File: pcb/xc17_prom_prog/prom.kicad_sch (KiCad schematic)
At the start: 28 parts, among them U14 SN74LVC8T245, U15 SN74LVC8T245, U16 SN74LVC8T245, U17 XC17xxx

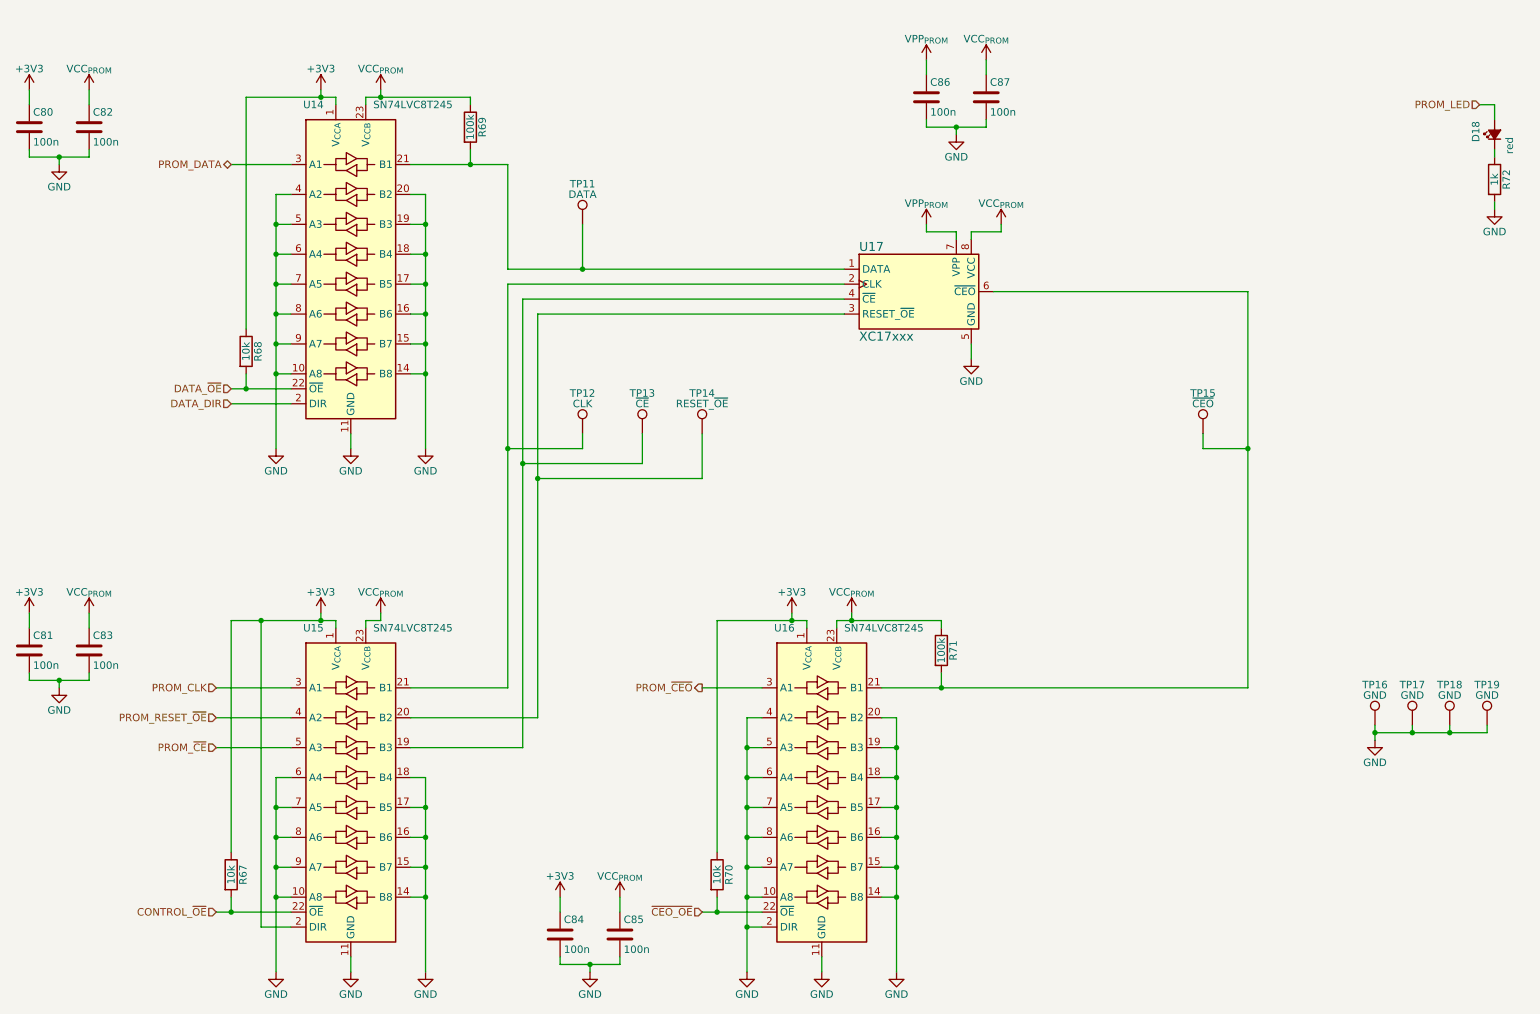
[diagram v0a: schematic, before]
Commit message: Fix MOSFETs
 * Block MOSFET body diodes by placing two MOSFETs in anti series.
 * Connect PROM LED to pin header.
 * Add transistors to actively pull PROM VCC and VPP low.
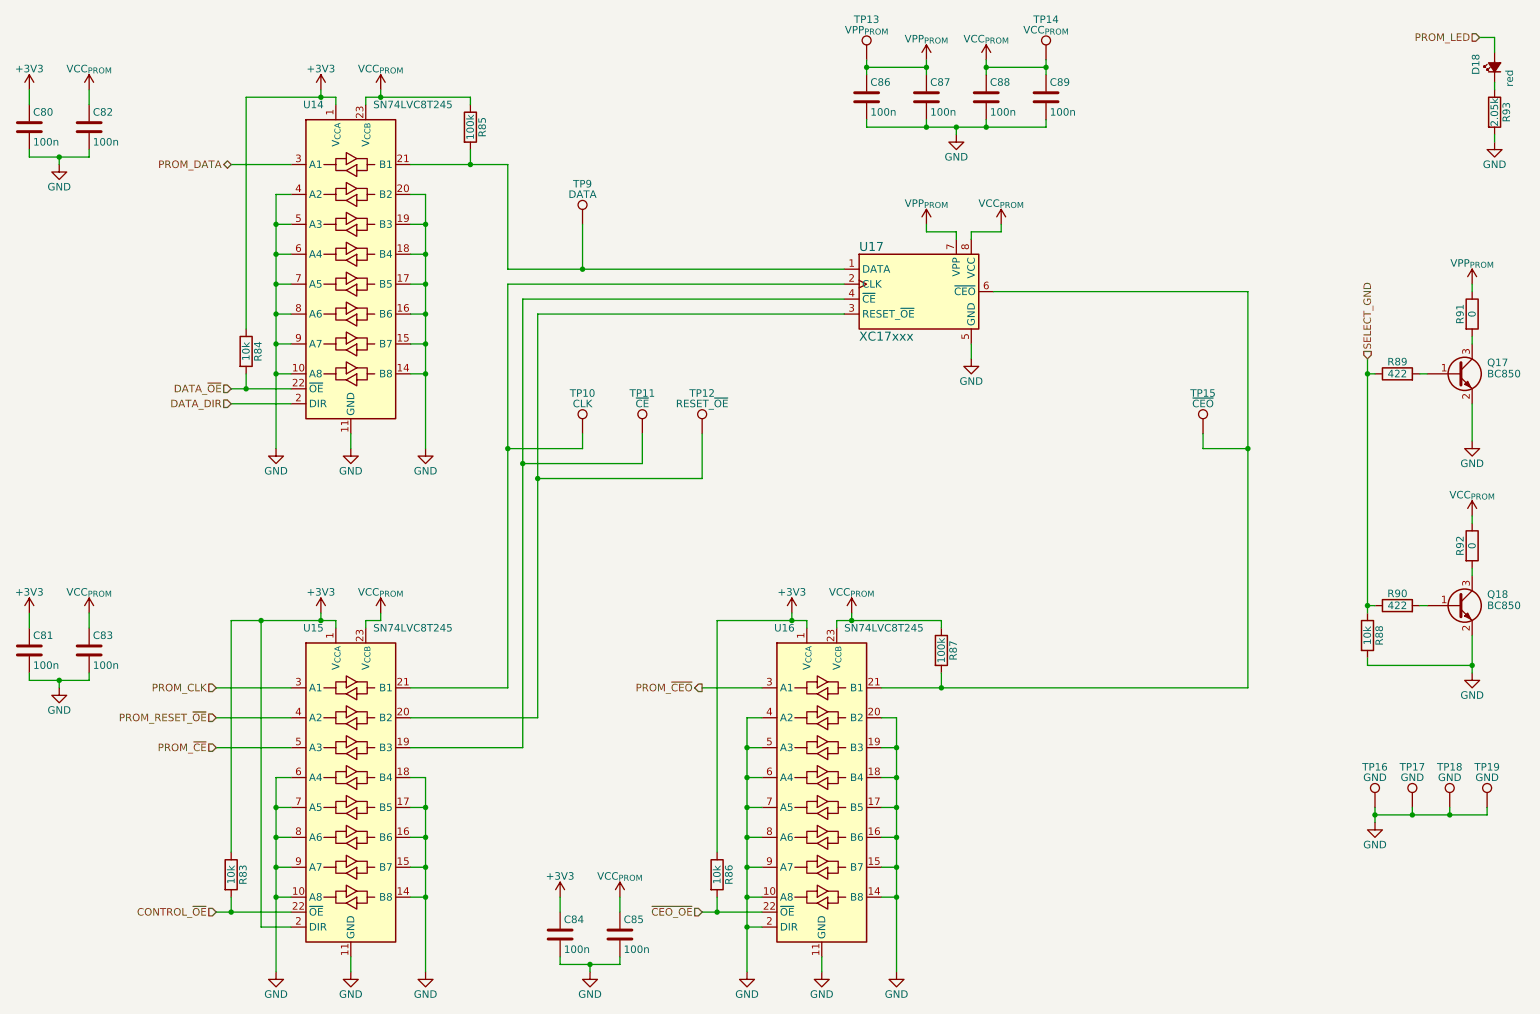
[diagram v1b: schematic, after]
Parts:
- added C86, C89: 100n, Capacitor_SMD:C_0603_1608Metric, symbol Device:C
- added Q17, Q18: BC850, Package_TO_SOT_SMD:SOT-23, symbol Transistor_BJT:BC850
- added R88: 10k, Resistor_SMD:R_0603_1608Metric, symbol Device:R
- added R89, R90: 422, Resistor_SMD:R_0603_1608Metric, symbol Device:R
- added R91, R92: 0, Resistor_SMD:R_0603_1608Metric, symbol Device:R
- added TP13: VPP_{PROM}, TestPoint:TestPoint_Keystone_5010-5014_Multipurpose, symbol Connector:TestPoint
- added TP14: VCC_{PROM}, TestPoint:TestPoint_Keystone_5010-5014_Multipurpose, symbol Connector:TestPoint
- R93: renamed from R72; value 1k -> 2.05k
- renumbered C86 to C87, C87 to C88, R67 to R83, R68 to R84, R69 to R85, R70 to R86, R71 to R87, TP12 to TP10, TP13 to TP11, TP14 to TP12, TP11 to TP9
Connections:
- net GND: now also C86.2, C89.2, Q17.2 (E), Q18.2 (E), R88.2
- net VCC_{PROM}: now also C89.1, R92.1, TP14.1
- net VPP_{PROM}: now also C86.1, R91.1, TP13.1
- new net: Q18.1 (B), R90.2
- new net: Q18.3 (C), R92.2
- new net: Q17.1 (B), R89.2
- new net: Q17.3 (C), R91.2
- new net SELECT_GND: R88.1, R89.1, R90.1
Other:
- moved on the sheet: D18, R93, TP16, TP17, TP18, TP19

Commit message: Implement more precise voltage controls
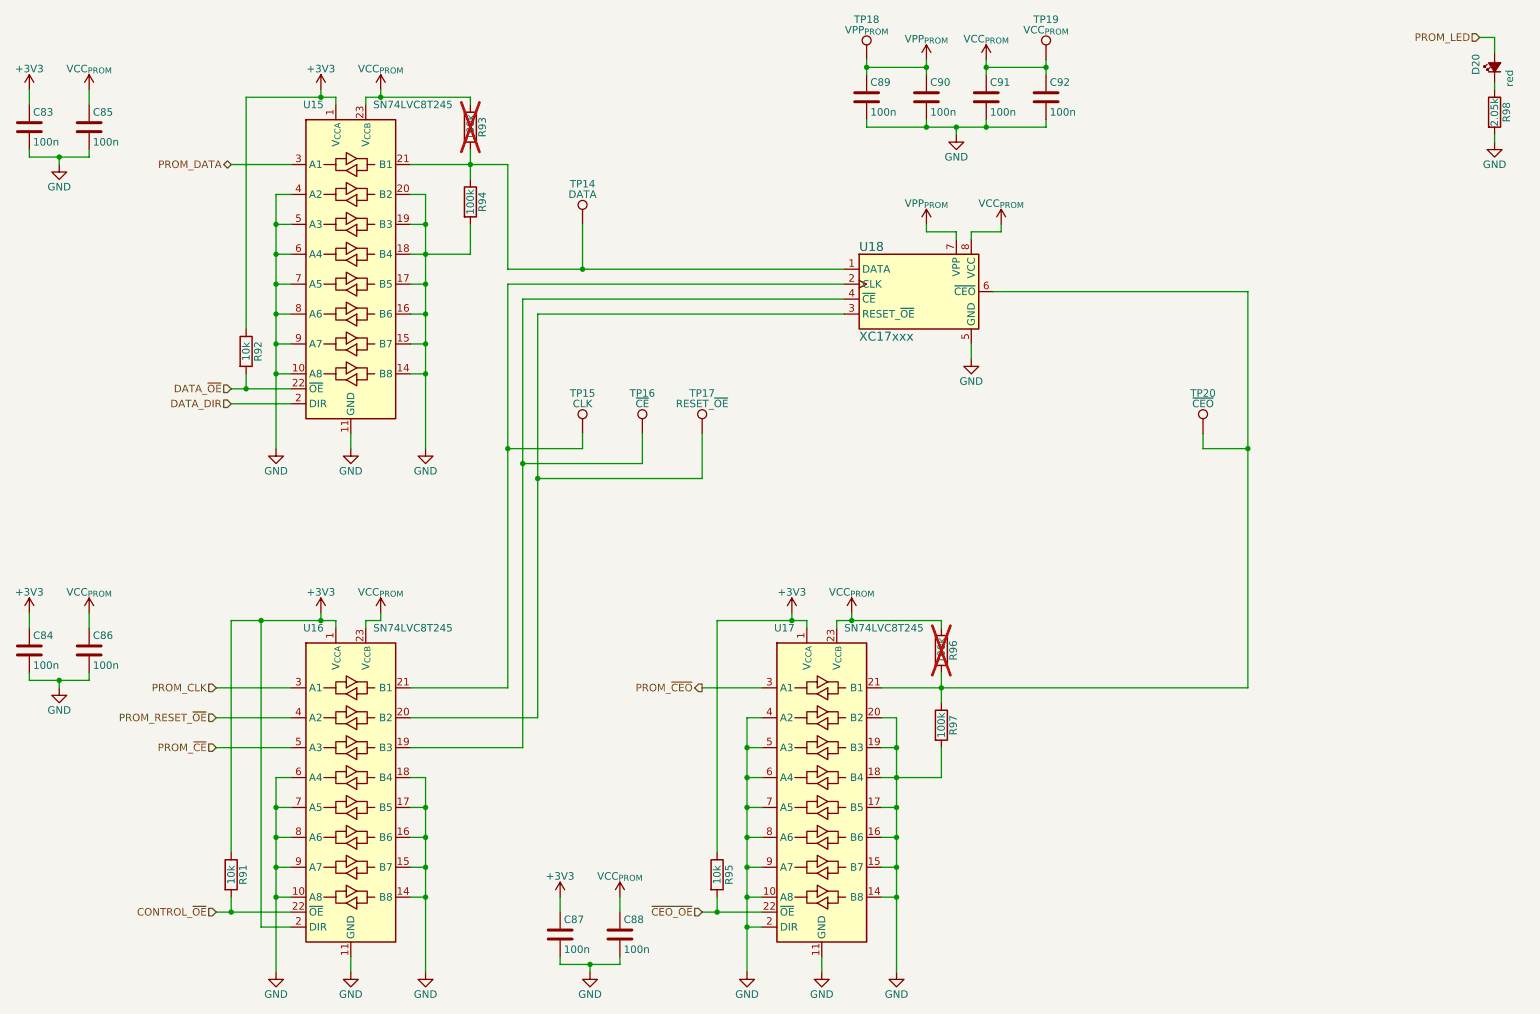
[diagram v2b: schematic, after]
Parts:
- removed Q17, Q18: BC850, Package_TO_SOT_SMD:SOT-23, symbol Transistor_BJT:BC850
- removed R88: 10k, Resistor_SMD:R_0603_1608Metric, symbol Device:R
- removed R89, R90: 422, Resistor_SMD:R_0603_1608Metric, symbol Device:R
- removed R91, R92: 0, Resistor_SMD:R_0603_1608Metric, symbol Device:R
- removed TP16, TP17, TP18, TP19: GND, TestPoint:TestPoint_Keystone_5010-5014_Multipurpose, symbol Connector:TestPoint
- added R94, R97: 100k, Resistor_SMD:R_0603_1608Metric, symbol Device:R
- R93: renamed from R85; now not fitted; now left out of the parts list
- R96: renamed from R87; now not fitted; now left out of the parts list
- renumbered C80 to C83, C81 to C84, C82 to C85, C83 to C86, C84 to C87, C85 to C88, C86 to C89, C87 to C90, C88 to C91, C89 to C92, D18 to D20, R83 to R91, R84 to R92, R86 to R95, R93 to R98, TP9 to TP14, TP10 to TP15, TP11 to TP16, TP12 to TP17, TP13 to TP18, TP14 to TP19, TP15 to TP20, U14 to U15, U15 to U16, U16 to U17, U17 to U18
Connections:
- net GND: now also R94.2, R97.2
- net at R93.2, TP14.1, U15.21 (B1)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: now also R94.1
- net at R96.2, TP20.1, U17.21 (B1)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: now also R97.1

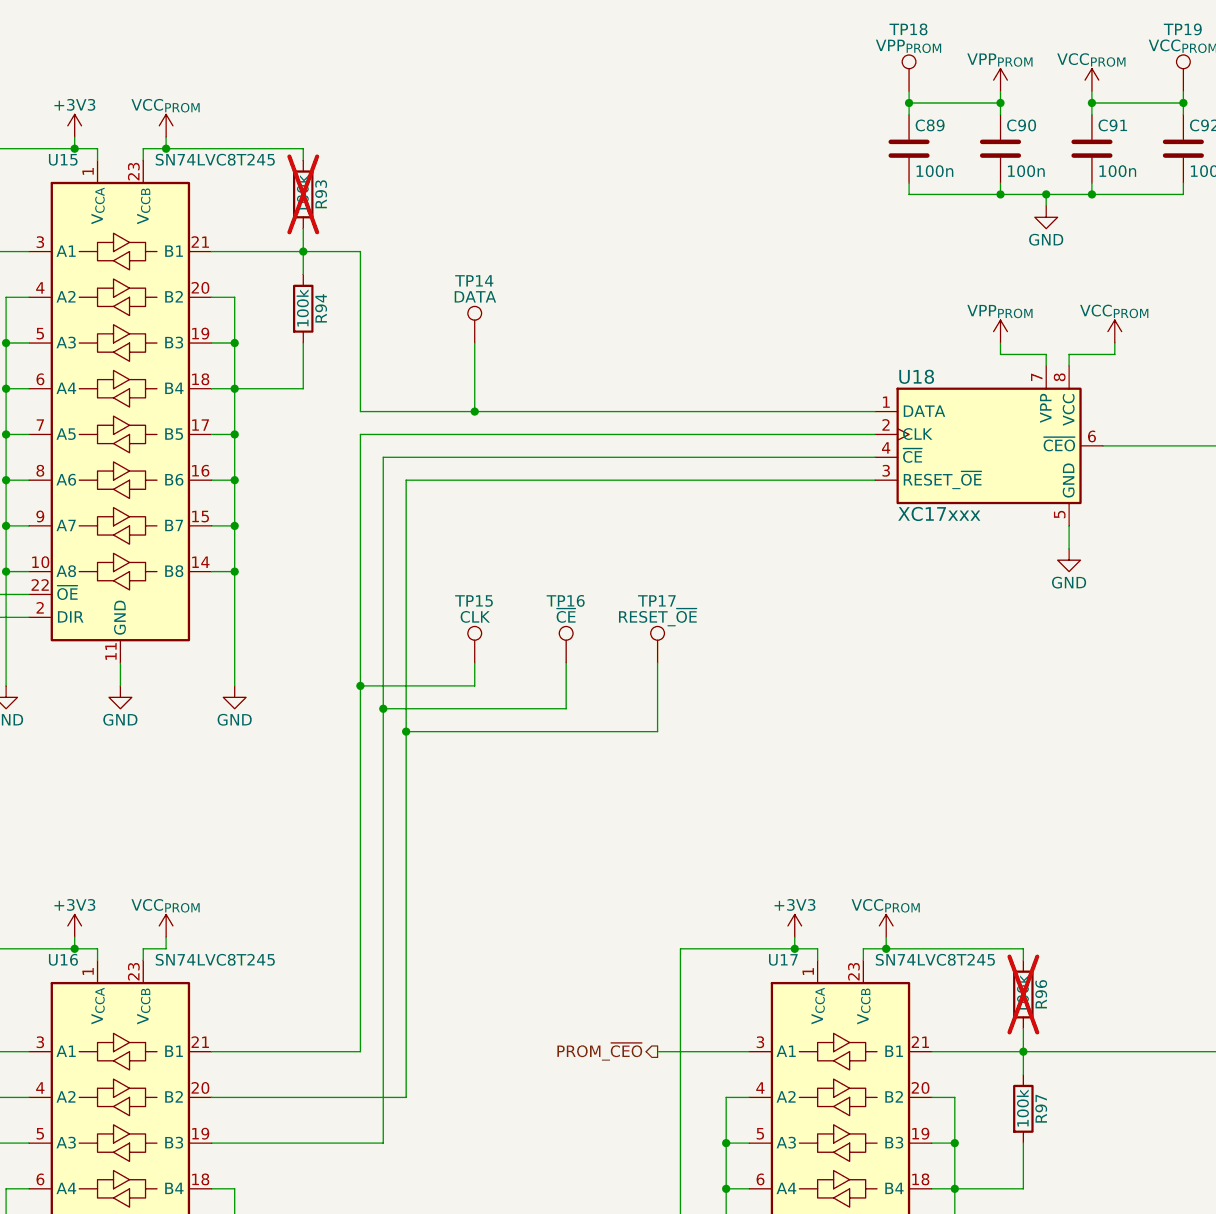
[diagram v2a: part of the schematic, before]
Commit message: Remove unused components
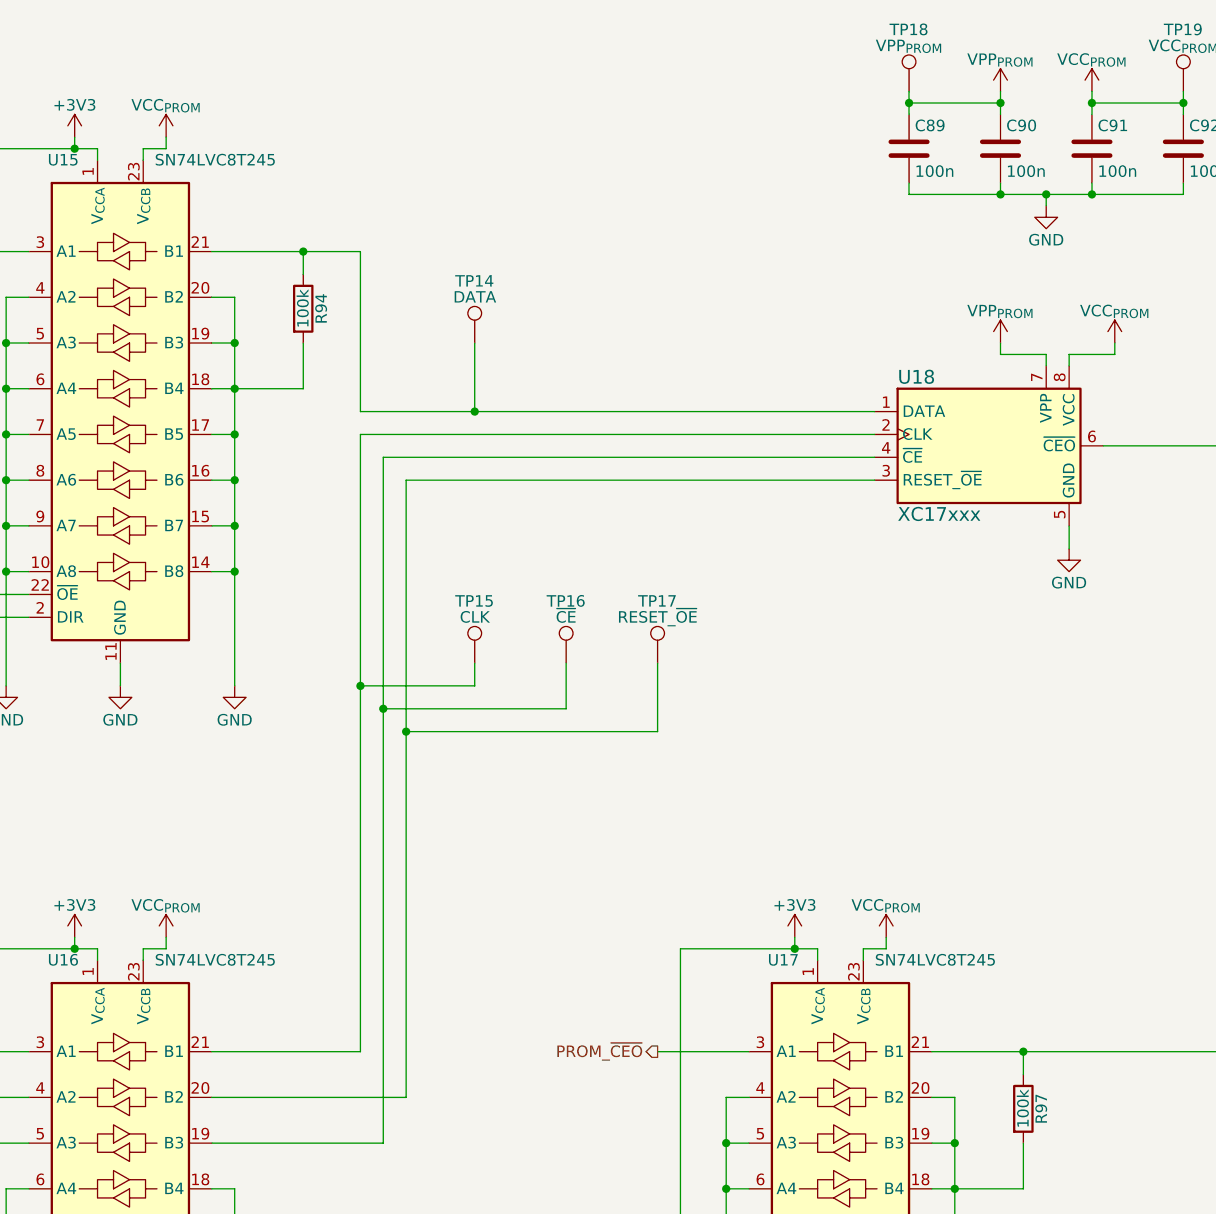
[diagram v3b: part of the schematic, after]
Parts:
- removed R93, R96: 100k, Resistor_SMD:R_0603_1608Metric, symbol Device:R
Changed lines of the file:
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@@
 	(title_block
 		(title "XC17xxx PROM Programmer")
-		(date "2024-12-08")
-		(rev "2")
+		(date "2025-01-29")
+		(rev "3")
 		(company "CC-BY-SA-4.0 Michael Singer")
 		(comment 1 "https://github.com/msinger/xc17_prom_prog/")
@@
 	)
 	(junction
-		(at 77.47 31.75)
-		(diameter 0)
-		(color 0 0 0 0)
-	)
-	(junction
 		(at 59.69 63.5)
 		(diameter 0)
@@
 	)
 	(junction
-		(at 157.48 120.65)
-		(diameter 0)
-		(color 0 0 0 0)
-	)
-	(junction
 		(at 59.69 152.4)
 		(diameter 0)
@@
 	(wire
 		(pts
-			(xy 172.72 132.08) (xy 172.72 129.54)
-		)
-		(stroke
-			(width 0)
-			(type default)
-		)
-	)
-	(wire
-		(pts
 			(xy 139.7 167.64) (xy 139.7 172.72)
 		)
@@
 	(wire
 		(pts
-			(xy 172.72 121.92) (xy 172.72 120.65)
-		)
-		(stroke
-			(width 0)
-			(type default)
-		)
-	)
-	(wire
-		(pts
 			(xy 82.55 68.58) (xy 85.09 68.58)
 		)
@@
 	(wire
 		(pts
-			(xy 172.72 120.65) (xy 157.48 120.65)
-		)
-		(stroke
-			(width 0)
-			(type default)
-		)
-	)
-	(wire
-		(pts
 			(xy 162.56 152.4) (xy 165.1 152.4)
 		)
@@
 	(wire
 		(pts
-			(xy 92.71 31.75) (xy 77.47 31.75)
-		)
-		(stroke
-			(width 0)
-			(type default)
-		)
-	)
-	(wire
-		(pts
 			(xy 165.1 162.56) (xy 165.1 157.48)
 		)
@@
 	(wire
 		(pts
-			(xy 92.71 43.18) (xy 92.71 40.64)
-		)
-		(stroke
-			(width 0)
-			(type default)
-		)
-	)
-	(wire
-		(pts
 			(xy 74.93 120.65) (xy 74.93 121.92)
 		)
@@
 	(wire
 		(pts
-			(xy 92.71 33.02) (xy 92.71 31.75)
-		)
-		(stroke
-			(width 0)
-			(type default)
-		)
-	)
-	(wire
-		(pts
 			(xy 104.14 96.52) (xy 104.14 137.16)
 		)
@@
 	)
 	(symbol
-		(lib_id "Device:R")
-		(at 172.72 125.73 0)
-		(unit 1)
-		(exclude_from_sim yes)
-		(in_bom no)
-		(on_board yes)
-		(dnp yes)
-		(property "Reference" "R96"
-			(at 174.752 125.73 90)
-			(effects
-				(font
-					(size 1.27 1.27)
-				)
-			)
-		)
-		(property "Value" "100k"
-			(at 172.72 125.73 90)
-			(effects
-				(font
-					(size 1.27 1.27)
-				)
-			)
-		)
-		(property "Footprint" "Resistor_SMD:R_0603_1608Metric"
-			(at 170.942 125.73 90)
-			(effects
-				(font
-					(size 1.27 1.27)
-				)
-				(hide yes)
-			)
-		)
-		(property "Datasheet" "~"
-			(at 172.72 125.73 0)
-			(effects
-				(font
-					(size 1.27 1.27)
-				)
-				(hide yes)
-			)
-		)
-		(property "Description" "Resistor"
-			(at 172.72 125.73 0)
-			(effects
-				(font
-					(size 1.27 1.27)
-				)
-				(hide yes)
-			)
-		)
-		(pin "1"
-		)
-		(pin "2"
-		)
-		(instances
-			(project "xc17_prom_prog"
-				(path "/3afea672-343d-4fc8-b012-067ac21cc0e9/43172acb-73d1-430e-bac0-31c53bbc6dab"
-					(reference "R96")
-					(unit 1)
-				)
-			)
-		)
-	)
-	(symbol
 		(lib_id "power:VCC")
 		(at 77.47 30.48 0)
@@
 					(unit 1)
 				)
-			)
-		)
-	)
-	(symbol
-		(lib_id "Device:R")
-		(at 92.71 36.83 0)
-		(unit 1)
-		(exclude_from_sim yes)
-		(in_bom no)
-		(on_board yes)
-		(dnp yes)
-		(property "Reference" "R93"
-			(at 94.742 36.83 90)
-			(effects
-				(font
-					(size 1.27 1.27)
-				)
-			)
-		)
-		(property "Value" "100k"
-			(at 92.71 36.83 90)
-			(effects
-				(font
-					(size 1.27 1.27)
-				)
-			)
-		)
-		(property "Footprint" "Resistor_SMD:R_0603_1608Metric"
-			(at 90.932 36.83 90)
-			(effects
-				(font
-					(size 1.27 1.27)
-				)
-				(hide yes)
-			)
-		)
-		(property "Datasheet" "~"
-			(at 92.71 36.83 0)
-			(effects
-				(font
-					(size 1.27 1.27)
-				)
-				(hide yes)
-			)
-		)
-		(property "Description" "Resistor"
-			(at 92.71 36.83 0)
-			(effects
-				(font
-					(size 1.27 1.27)
-				)
-				(hide yes)
-			)
-		)
-		(pin "1"
-		)
-		(pin "2"
-		)
-		(instances
-			(project "xc17_prom_prog"
-				(path "/3afea672-343d-4fc8-b012-067ac21cc0e9/43172acb-73d1-430e-bac0-31c53bbc6dab"
-					(reference "R93")
-					(unit 1)
-				)
